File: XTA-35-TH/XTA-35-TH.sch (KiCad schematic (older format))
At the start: 36 parts, among them J1 XTA_Connector, J2 XTA Power, J3 LED, J4 SD0, J5 SD1, J6 DEBUG, SW1 Config, SW2 Boot Internal, SW3 Reset, U1 74LVC245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

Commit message: Remove serial config jumpers/IC. Just connect the boot override button. We will instead use USB serial to access a configuration menu and save configured options to the flash memory.
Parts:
- removed R5, R6, R7, R8, R9: 10K, Resistor_SMD:R_1206_3216Metric, symbol Device:R
- removed SW1: Config, 00Common:SW_DIP_SPSTx04, symbol Switch:SW_DIP_x04
- removed U4: 74HC165, Package_DIP:DIP-16_W7.62mm_Socket, symbol 74xx:74HC165
- SW2: value Boot Internal -> Boot Override
- U2: symbol 00Custom:74LS245_One_Way -> 00Custom:74LS245_One_Way_Reverse
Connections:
- net CFG_DATA is gone; now on net BOOT_OVERRIDE: U5.9 (GP6)
- net VBUS: now reaches U5.40 (VBUS)
- net CFG_CLK renamed ~DRIVE_ACTIVE~_3V3
- net CFG_LATCH renamed SD1_CS
- no-connect marks 10 -> 9
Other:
- note removed: "CONFIGURATION"
- moved on the sheet: J6, R4, SW2, SW3, U5

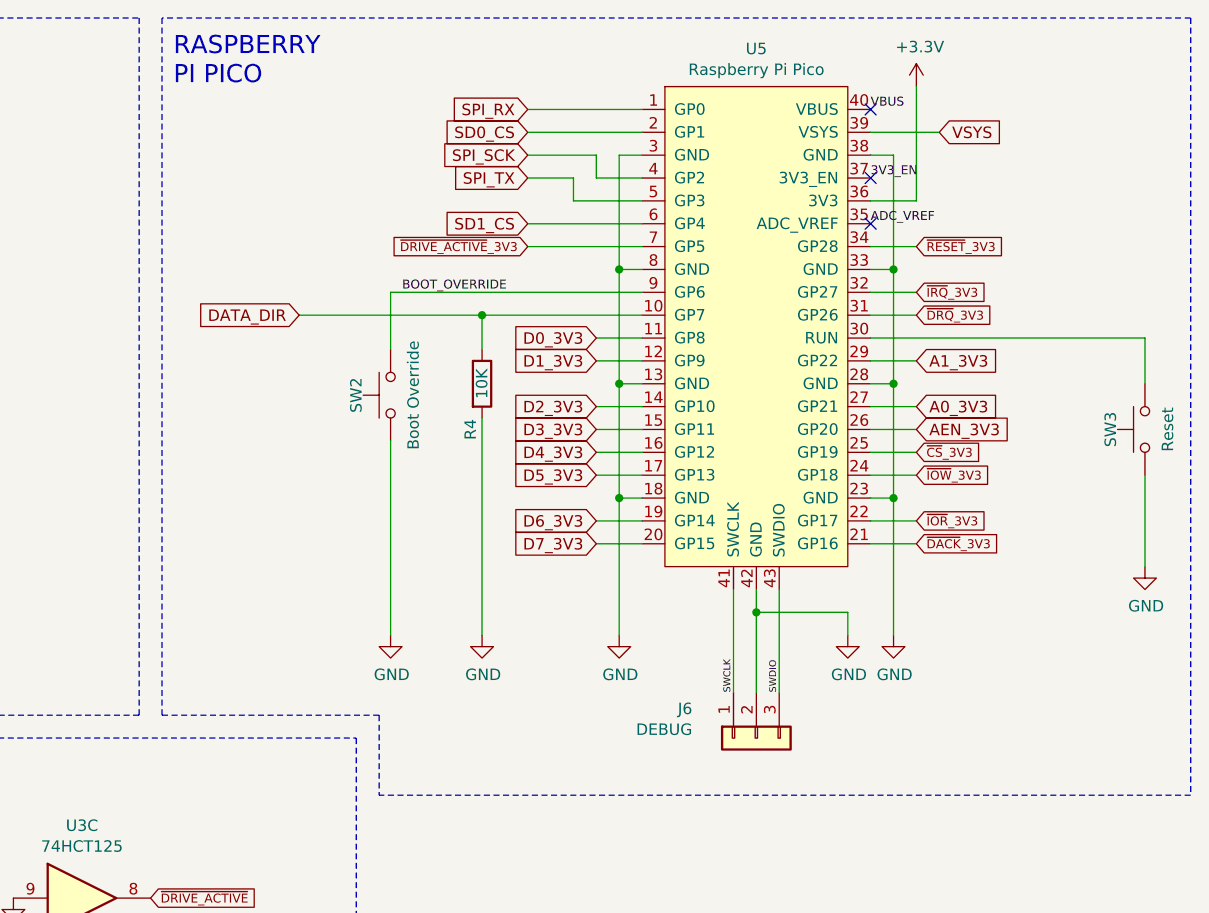
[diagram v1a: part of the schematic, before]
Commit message: Shited pin positions so DRQ and IRQ immediately follow address lines.
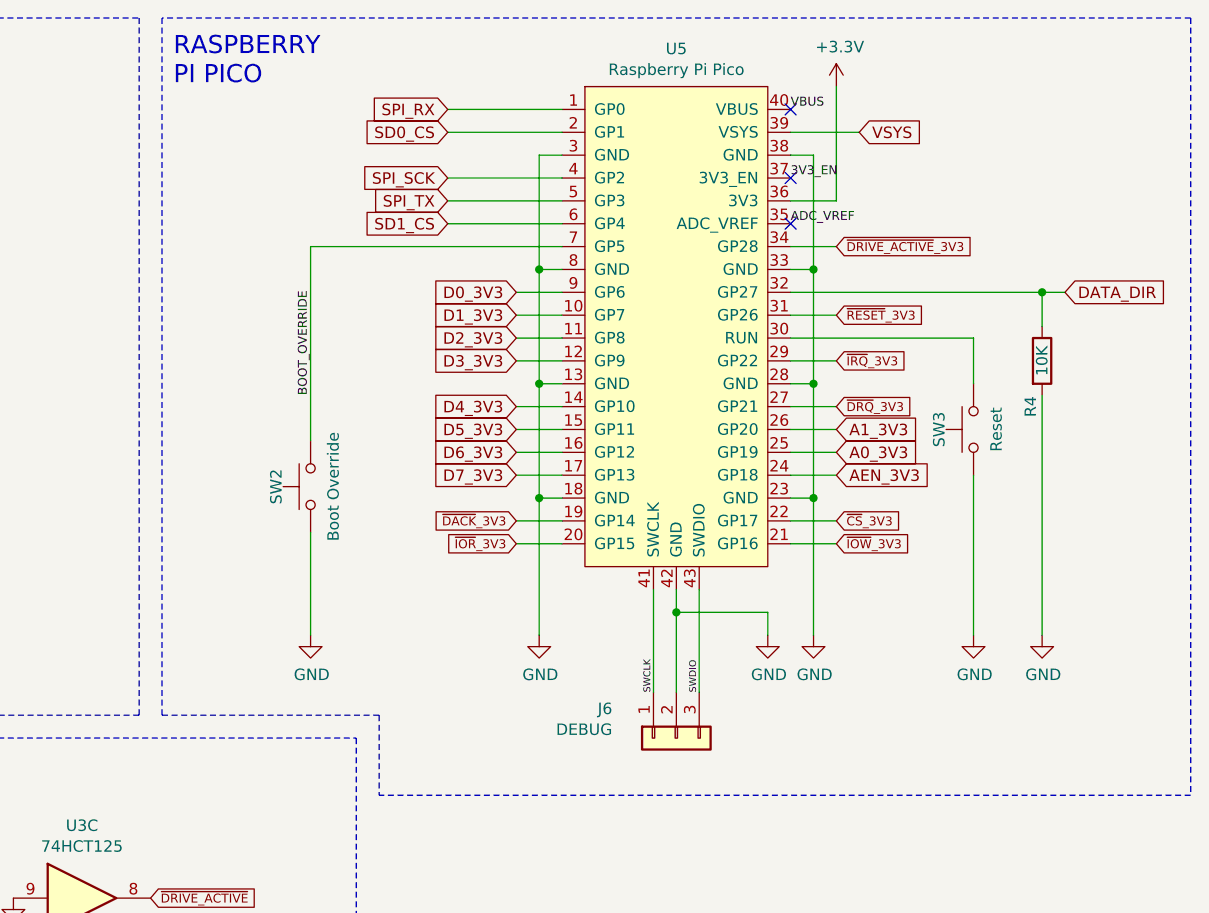
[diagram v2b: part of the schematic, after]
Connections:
- net A0_3V3: now also U5.25 (GP19); no longer U5.27 (GP21)
- net A1_3V3: now also U5.26 (GP20); no longer U5.29 (GP22)
- net AEN_3V3: now also U5.24 (GP18); no longer U5.26 (GP20)
- net BOOT_OVERRIDE: now also U5.7 (GP5); no longer U5.9 (GP6)
- net D0_3V3: now also U5.9 (GP6); no longer U5.11 (GP8)
- net D1_3V3: now also U5.10 (GP7); no longer U5.12 (GP9)
- net D2_3V3: now also U5.11 (GP8); no longer U5.14 (GP10)
- net D3_3V3: now also U5.12 (GP9); no longer U5.15 (GP11)
- net D4_3V3: now also U5.14 (GP10); no longer U5.16 (GP12)
- net D5_3V3: now also U5.15 (GP11); no longer U5.17 (GP13)
- net D6_3V3: now also U5.16 (GP12); no longer U5.19 (GP14)
- net D7_3V3: now also U5.17 (GP13); no longer U5.20 (GP15)
- net DATA_DIR: now also U5.32 (GP27); no longer U5.10 (GP7)
- net ~CS~_3V3: now also U5.22 (GP17); no longer U5.25 (GP19)
- net ~DACK~_3V3: now also U5.19 (GP14); no longer U5.21 (GP16)
- net ~DRIVE_ACTIVE~_3V3: now also U5.34 (GP28); no longer U5.7 (GP5)
- net ~DRQ~_3V3: now also U5.27 (GP21); no longer U5.31 (GP26)
- net ~IOR~_3V3: now also U5.20 (GP15); no longer U5.22 (GP17)
- net ~IOW~_3V3: now also U5.21 (GP16); no longer U5.24 (GP18)
- net ~IRQ~_3V3: now also U5.29 (GP22); no longer U5.32 (GP27)
- net ~RESET~_3V3: now also U5.31 (GP26); no longer U5.34 (GP28)
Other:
- moved on the sheet: J6, R4, SW2, SW3, U5

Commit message: Update board and schematic pdf to match latest changes.
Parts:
- removed C4: 0.1uF, Capacitor_SMD:C_1206_3216Metric, symbol Device:C
- renumbered SW2 to SW1, SW3 to SW2
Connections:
- net ~DRIVE_ACTIVE~_3V3: now also U5.31 (GP26); no longer U5.34 (GP28)
- net ~RESET~_3V3: now also U5.34 (GP28); no longer U5.31 (GP26)
- net RUN: now reaches SW2.1, U5.30 (RUN)
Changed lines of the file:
@@
 NoConn ~ 9350 1450
 $Comp
-L Switch:SW_Push SW3
+L Switch:SW_Push SW2
 U 1 1 61708BD1
 P 10150 2350
-F 0 "SW3" H 10150 2500 50  0000 C CNN
+F 0 "SW2" H 10150 2500 50  0000 C CNN
 F 1 "Reset" H 10150 2250 50  0000 C CNN
 F 2 "Button_Switch_THT:SW_PUSH_6mm" H 10150 2550 50  0001 C CNN
@@
 Text GLabel 9550 2850 2    39   Input ~ 0
 ~IOW~_3V3
-Text GLabel 9550 1850 2    39   Input ~ 0
+Text GLabel 9550 1550 2    39   Input ~ 0
 ~RESET~_3V3
 Wire Wire Line
@@
 $EndComp
 $Comp
-L power:+3.3V #PWR032
-U 1 1 61C70A31
-P 4850 6800
-F 0 "#PWR032" H 4850 6650 50  0001 C CNN
-F 1 "+3.3V" H 4865 6973 50  0000 C CNN
-F 2 "" H 4850 6800 50  0001 C CNN
-F 3 "" H 4850 6800 50  0001 C CNN
-	1    4850 6800
-	1    0    0    -1
-$EndComp
-$Comp
-L Device:C C4
-U 1 1 61C7BDDB
-P 4850 6950
-F 0 "C4" H 4965 6996 50  0000 L CNN
-F 1 "0.1uF" H 4965 6905 50  0000 L CNN
-F 2 "Capacitor_SMD:C_1206_3216Metric" H 4888 6800 50  0001 C CNN
-F 3 "~" H 4850 6950 50  0001 C CNN
-F 4 " C24497" H 4850 6950 50  0001 C CNN "LCSC"
-	1    4850 6950
-	1    0    0    -1
-$EndComp
-$Comp
-L power:GND #PWR035
-U 1 1 61C7C481
-P 4850 7100
-F 0 "#PWR035" H 4850 6850 50  0001 C CNN
-F 1 "GND" H 4855 6927 50  0000 C CNN
-F 2 "" H 4850 7100 50  0001 C CNN
-F 3 "" H 4850 7100 50  0001 C CNN
-	1    4850 7100
-	1    0    0    -1
-$EndComp
-$Comp
 L power:+5V #PWR034
 U 1 1 61C87915
@@
 Text GLabel 3700 4600 2    50   Input ~ 0
 A0
-Text GLabel 9550 1550 2    39   Input ~ 0
+Text GLabel 9550 1850 2    39   Input ~ 0
 ~DRIVE_ACTIVE~_3V3
 Wire Wire Line
@@
 	7250 2800 7250 3250
 $Comp
-L Switch:SW_Push SW2
+L Switch:SW_Push SW1
 U 1 1 619AC049
 P 7250 2600
-F 0 "SW2" H 7250 2750 50  0000 C CNN
+F 0 "SW1" H 7250 2750 50  0000 C CNN
 F 1 "Boot Override" H 7250 2500 50  0000 C CNN
 F 2 "Button_Switch_THT:SW_PUSH_6mm" H 7250 2800 50  0001 C CNN
@@
 Wire Wire Line
 	10450 1750 9350 1750
+Text Label 10000 1950 0    39   ~ 0
+RUN
 $EndSCHEMATC

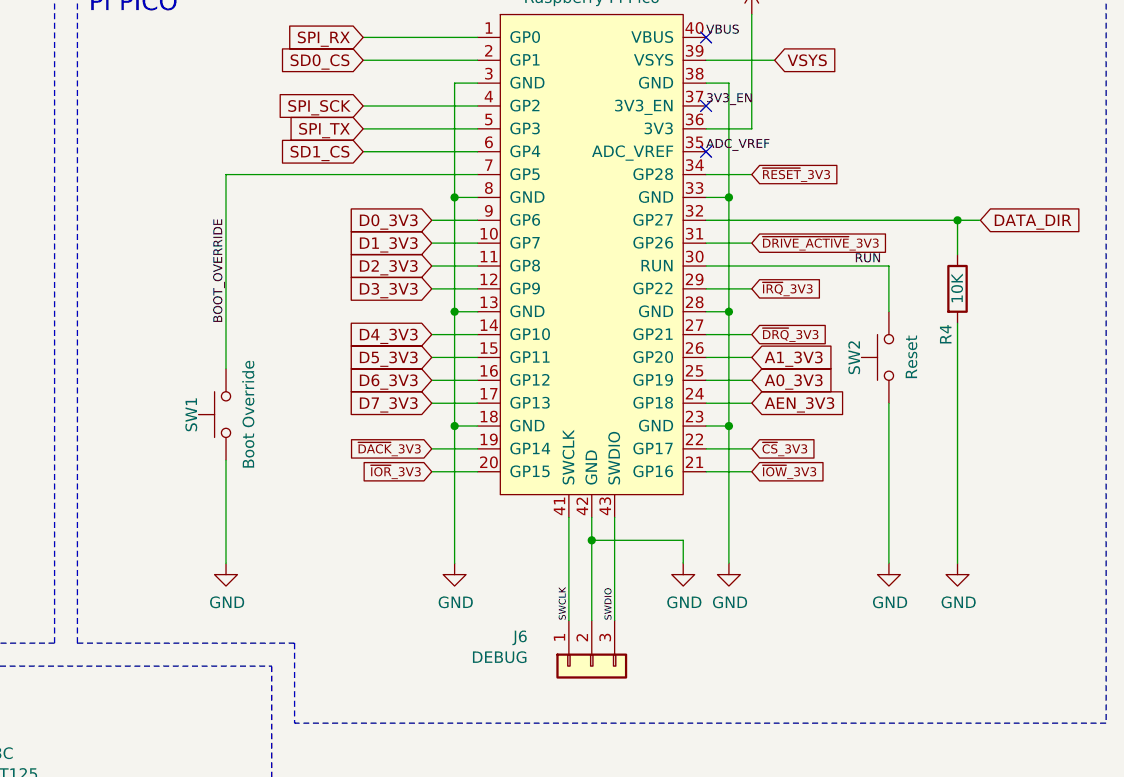
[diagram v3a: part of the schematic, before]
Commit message: More pin reassignments.
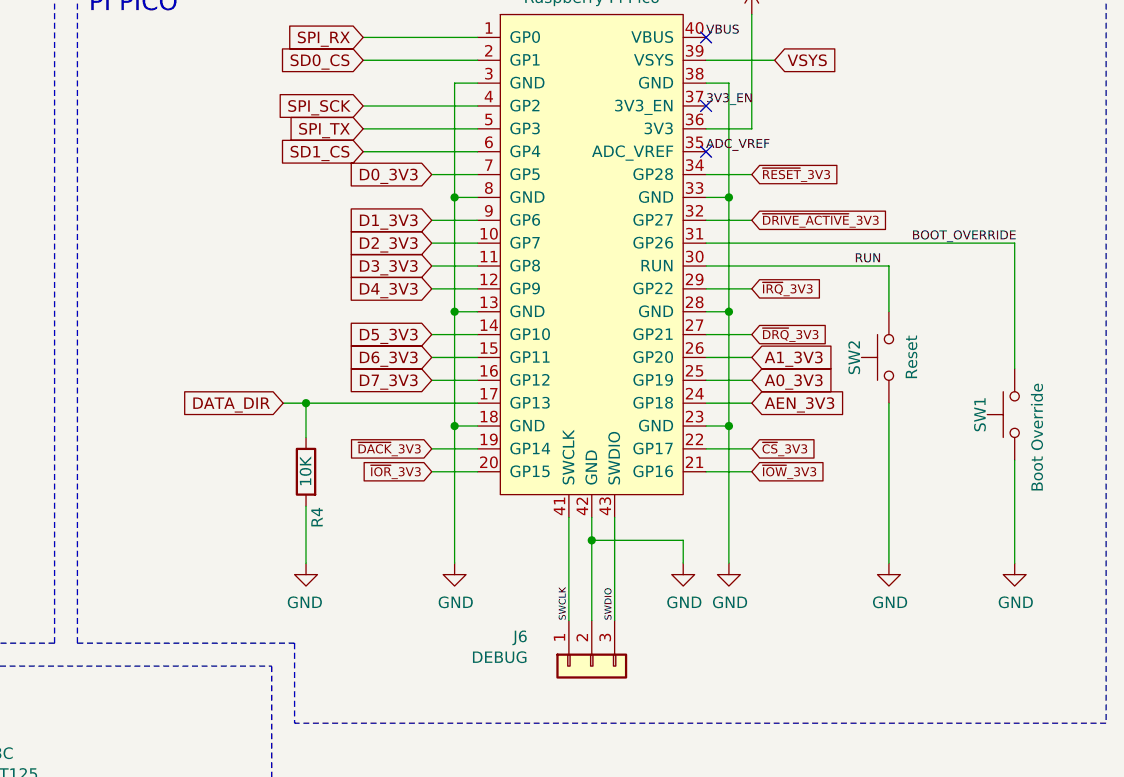
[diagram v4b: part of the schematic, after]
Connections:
- net BOOT_OVERRIDE: now also U5.31 (GP26); no longer U5.7 (GP5)
- net D0_3V3: now also U5.7 (GP5); no longer U5.9 (GP6)
- net D1_3V3: now also U5.9 (GP6); no longer U5.10 (GP7)
- net D2_3V3: now also U5.10 (GP7); no longer U5.11 (GP8)
- net D3_3V3: now also U5.11 (GP8); no longer U5.12 (GP9)
- net D4_3V3: now also U5.12 (GP9); no longer U5.14 (GP10)
- net D5_3V3: now also U5.14 (GP10); no longer U5.15 (GP11)
- net D6_3V3: now also U5.15 (GP11); no longer U5.16 (GP12)
- net D7_3V3: now also U5.16 (GP12); no longer U5.17 (GP13)
- net DATA_DIR: now also U5.17 (GP13); no longer U5.32 (GP27)
- net ~DRIVE_ACTIVE~_3V3: now also U5.32 (GP27); no longer U5.31 (GP26)
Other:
- moved on the sheet: R4, SW1
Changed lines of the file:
@@
 Wire Wire Line
 	10150 3250 10150 2550
+Text GLabel 8150 1550 0    50   Input ~ 0
+D0_3V3
 Text GLabel 8150 1750 0    50   Input ~ 0
-D0_3V3
+D1_3V3
 Text GLabel 8150 1850 0    50   Input ~ 0
-D1_3V3
+D2_3V3
 Text GLabel 8150 1950 0    50   Input ~ 0
-D2_3V3
+D3_3V3
 Text GLabel 8150 2050 0    50   Input ~ 0
-D3_3V3
+D4_3V3
 Text GLabel 8150 2250 0    50   Input ~ 0
-D4_3V3
+D5_3V3
 Text GLabel 8150 2350 0    50   Input ~ 0
-D5_3V3
+D6_3V3
 Text GLabel 8150 2450 0    50   Input ~ 0
-D6_3V3
-Text GLabel 8150 2550 0    50   Input ~ 0
 D7_3V3
 Text GLabel 9550 2450 2    50   Input ~ 0
@@
 Wire Wire Line
 	8350 2450 8150 2450
-Wire Wire Line
-	8150 2550 8350 2550
 Wire Wire Line
 	9550 2550 9350 2550
@@
 	9550 2250 9350 2250
 Wire Wire Line
-	10550 1750 10450 1750
+	7500 2550 7600 2550
 Wire Wire Line
 	9550 2050 9350 2050
@@
 Text Notes 6650 850  0    79   ~ 0
 RASPBERRY\nPI PICO
-Wire Notes Line
-	11100 550  6600 550
 Wire Notes Line
 	6600 550  6600 3600
@@
 Wire Wire Line
 	7850 950  8350 950
-Wire Wire Line
-	9350 1850 9550 1850
 Text GLabel 3700 4600 2    50   Input ~ 0
 A0
-Text GLabel 9550 1850 2    39   Input ~ 0
-~DRIVE_ACTIVE~_3V3
 Wire Wire Line
 	7850 1450 8350 1450
 Text Label 9350 950  0    39   ~ 0
 VBUS
-Text Label 7250 2200 1    39   ~ 0
-BOOT_OVERRIDE
+$Comp
+L Device:R R4
+U 1 1 61A94ADE
+P 7600 2850
+F 0 "R4" V 7550 2650 50  0000 C CNN
+F 1 "10K" V 7600 2850 50  0000 C CNN
+F 2 "Resistor_SMD:R_1206_3216Metric" V 7530 2850 50  0001 C CNN
+F 3 "~" H 7600 2850 50  0001 C CNN
+F 4 "C17902" V 7600 2850 50  0001 C CNN "LCSC"
+	1    7600 2850
+	-1   0    0    -1
+$EndComp
+Wire Wire Line
+	7600 3000 7600 3250
+Wire Wire Line
+	7600 2700 7600 2550
+$Comp
+L power:GND #PWR010
+U 1 1 61A95646
+P 7600 3250
+F 0 "#PWR010" H 7600 3000 50  0001 C CNN
+F 1 "GND" H 7605 3077 50  0000 C CNN
+F 2 "" H 7600 3250 50  0001 C CNN
+F 3 "" H 7600 3250 50  0001 C CNN
+	1    7600 3250
+	-1   0    0    -1
+$EndComp
+Text GLabel 7500 2550 0    50   Input ~ 0
+DATA_DIR
+Wire Notes Line
+	7550 3600 6600 3600
+Wire Notes Line
+	6500 3600 3950 3600
+Wire Wire Line
+	8150 1750 8350 1750
+Wire Wire Line
+	8150 1850 8350 1850
+Wire Wire Line
+	7850 1350 8350 1350
+Wire Wire Line
+	7850 1250 8350 1250
+Connection ~ 7600 2550
+Text Label 10000 1950 0    39   ~ 0
+RUN
+Wire Wire Line
+	8350 1550 8150 1550
+Wire Wire Line
+	7600 2550 8350 2550
+Wire Notes Line
+	11100 550  6600 550
+$Comp
+L Switch:SW_Push SW1
+U 1 1 619AC049
+P 10700 2600
+F 0 "SW1" H 10700 2750 50  0000 C CNN
+F 1 "Boot Override" H 10800 2500 50  0000 C CNN
+F 2 "Button_Switch_THT:SW_PUSH_6mm" H 10700 2800 50  0001 C CNN
+F 3 "~" H 10700 2800 50  0001 C CNN
+	1    10700 2600
+	0    -1   1    0
+$EndComp
+Wire Wire Line
+	10700 2800 10700 3250
 $Comp
 L power:GND #PWR0108
 U 1 1 61AEF52F
-P 7250 3250
-F 0 "#PWR0108" H 7250 3000 50  0001 C CNN
-F 1 "GND" H 7255 3077 50  0000 C CNN
-F 2 "" H 7250 3250 50  0001 C CNN
-F 3 "" H 7250 3250 50  0001 C CNN
-	1    7250 3250
-	1    0    0    -1
-$EndComp
-Wire Wire Line
-	7250 2800 7250 3250
-$Comp
-L Switch:SW_Push SW1
-U 1 1 619AC049
-P 7250 2600
-F 0 "SW1" H 7250 2750 50  0000 C CNN
-F 1 "Boot Override" H 7250 2500 50  0000 C CNN
-F 2 "Button_Switch_THT:SW_PUSH_6mm" H 7250 2800 50  0001 C CNN
-F 3 "~" H 7250 2800 50  0001 C CNN
-	1    7250 2600
-	0    -1   1    0
-$EndComp
-$Comp
-L Device:R R4
-U 1 1 61A94ADE
-P 10450 2050
-F 0 "R4" V 10400 1850 50  0000 C CNN
-F 1 "10K" V 10450 2050 50  0000 C CNN
-F 2 "Resistor_SMD:R_1206_3216Metric" V 10380 2050 50  0001 C CNN
-F 3 "~" H 10450 2050 50  0001 C CNN
-F 4 "C17902" V 10450 2050 50  0001 C CNN "LCSC"
-	1    10450 2050
-	1    0    0    -1
-$EndComp
-Wire Wire Line
-	10450 2200 10450 3250
-Wire Wire Line
-	10450 1900 10450 1750
-$Comp
-L power:GND #PWR010
-U 1 1 61A95646
-P 10450 3250
-F 0 "#PWR010" H 10450 3000 50  0001 C CNN
-F 1 "GND" H 10455 3077 50  0000 C CNN
-F 2 "" H 10450 3250 50  0001 C CNN
-F 3 "" H 10450 3250 50  0001 C CNN
-	1    10450 3250
-	1    0    0    -1
-$EndComp
-Text GLabel 10550 1750 2    50   Input ~ 0
-DATA_DIR
-Wire Notes Line
-	7550 3600 6600 3600
-Wire Notes Line
-	6500 3600 3950 3600
-Wire Wire Line
-	8150 1750 8350 1750
-Wire Wire Line
-	8150 1850 8350 1850
-Wire Wire Line
-	7850 1350 8350 1350
-Wire Wire Line
-	7850 1250 8350 1250
-Wire Wire Line
-	7250 1550 7250 2400
-Wire Wire Line
-	7250 1550 8350 1550
-Connection ~ 10450 1750
-Wire Wire Line
-	10450 1750 9350 1750
-Text Label 10000 1950 0    39   ~ 0
-RUN
+P 10700 3250
+F 0 "#PWR0108" H 10700 3000 50  0001 C CNN
+F 1 "GND" H 10705 3077 50  0000 C CNN
+F 2 "" H 10700 3250 50  0001 C CNN
+F 3 "" H 10700 3250 50  0001 C CNN
+	1    10700 3250
+	1    0    0    -1
+$EndComp
+Text Label 10250 1850 0    39   ~ 0
+BOOT_OVERRIDE
+Wire Wire Line
+	9350 1750 9550 1750
+Text GLabel 9550 1750 2    39   Input ~ 0
+~DRIVE_ACTIVE~_3V3
+Wire Wire Line
+	9350 1850 10700 1850
+Wire Wire Line
+	10700 1850 10700 2400
 $EndSCHEMATC
